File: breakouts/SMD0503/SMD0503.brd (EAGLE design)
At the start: 13.6 x 17.9 mm, 8 parts

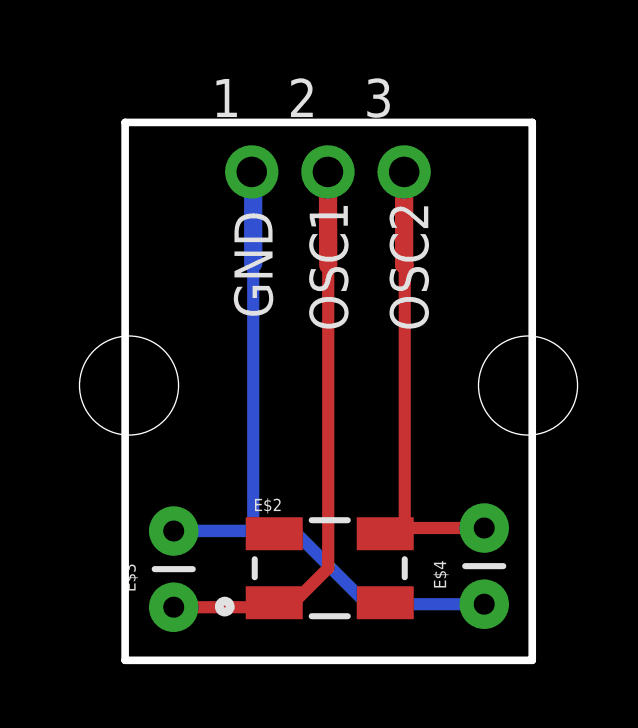
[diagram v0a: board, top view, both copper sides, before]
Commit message: SMD0503 - converted entirely to SMD components
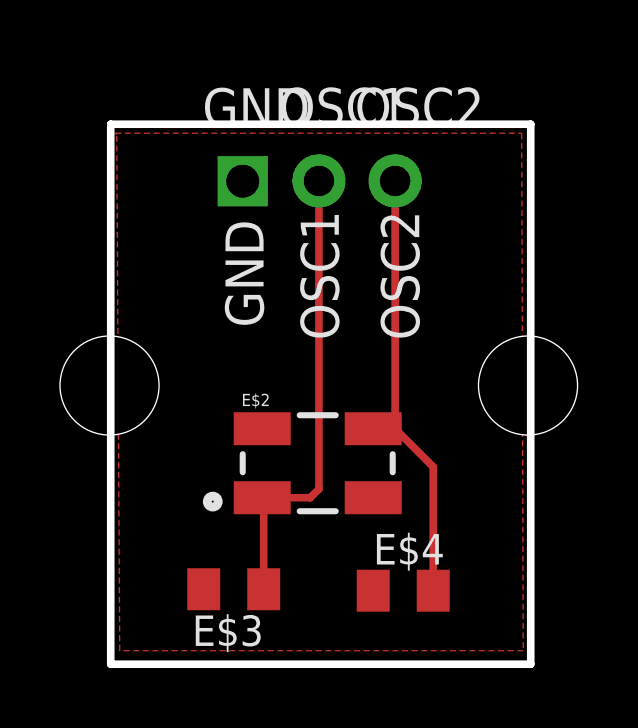
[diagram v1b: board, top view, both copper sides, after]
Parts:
- removed 1, 2, 3: (no value), adafruit:1X01-CLEANBIG
- added GND: (no value), adafruit_4u:1X01
- added OSC1, OSC2: (no value), adafruit:1X01-CLEANBIG
- E$3, E$4: device SparkFun:CAP-PTH-SMALL -> adafruit:C0805K
- moved E$2 3.52 mm to (14.9, 11.7)
- moved E$4 2.74 mm to (17.8, 7.45), turned to 0 degrees
- moved E$3 2.09 mm to (12.1, 7.50), turned to 180 degrees
- moved JP4 0.65 mm to (7.96, 14.3)
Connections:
- net GND: now also GND.1; no longer 1.1
- net OSC1: now also OSC1.1; no longer 2.1
- net OSC2: now also OSC2.1; no longer 3.1
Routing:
- net GND: track 26.0 -> 0.00 mm
- net OSC1: track 18.9 -> 15.4 mm
- added copper zone on layer 1, net GND
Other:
- board size 13.6 x 17.9 mm -> 14 x 18 mm
- board text added: "SMD0503"
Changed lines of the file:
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@@
 <layer number="45" name="Holes" color="7" fill="1" visible="no" active="yes"/>
 <layer number="46" name="Milling" color="3" fill="1" visible="no" active="yes"/>
-<layer number="47" name="Measures" color="7" fill="1" visible="no" active="yes"/>
+<layer number="47" name="Measures" color="7" fill="1" visible="yes" active="yes"/>
 <layer number="48" name="Document" color="7" fill="1" visible="yes" active="yes"/>
 <layer number="49" name="Reference" color="7" fill="1" visible="yes" active="yes"/>
@@
 <board>
 <plain>
-<wire x1="8.48" y1="5.13" x2="8.48" y2="23.06" width="0.254" layer="20"/>
-<wire x1="8.48" y1="23.06" x2="22.05" y2="23.06" width="0.254" layer="20"/>
-<wire x1="22.05" y1="23.06" x2="22.05" y2="5.13" width="0.254" layer="20"/>
-<wire x1="22.05" y1="5.13" x2="8.48" y2="5.13" width="0.254" layer="20"/>
-<text x="12.125" y="20.12" size="1.27" layer="121" font="vector" ratio="15" rot="R270">GND</text>
-<text x="14.635" y="20.42" size="1.27" layer="121" font="vector" ratio="15" rot="R270">OSC1</text>
-<text x="17.315" y="20.42" size="1.27" layer="121" font="vector" ratio="15" rot="R270">OSC2</text>
-<text x="19.93" y="18.03" size="1.27" layer="122" font="vector" rot="MR0">quilix.com</text>
+<wire x1="8" y1="5" x2="8" y2="23" width="0.254" layer="20"/>
+<wire x1="8" y1="23" x2="22" y2="23" width="0.254" layer="20"/>
+<wire x1="22" y1="23" x2="22" y2="5" width="0.254" layer="20"/>
+<wire x1="22" y1="5" x2="8" y2="5" width="0.254" layer="20"/>
+<text x="11.825" y="19.82" size="1.27" layer="121" font="vector" ratio="15" rot="R270">GND</text>
+<text x="14.335" y="20.12" size="1.27" layer="121" font="vector" ratio="15" rot="R270">OSC1</text>
+<text x="17.015" y="20.12" size="1.27" layer="121" font="vector" ratio="15" rot="R270">OSC2</text>
+<text x="19.63" y="17.93" size="1.27" layer="122" font="vector" ratio="10" rot="MR0">quilix.com</text>
+<text x="18.98" y="7.48" size="1.27" layer="122" font="vector" ratio="10" rot="MR0">SMD0503</text>
+<dimension x1="8" y1="23.06" x2="22" y2="23.06" x3="15" y3="28.3" layer="47"/>
+<dimension x1="8" y1="5.13" x2="15" y2="5.1" x3="11.47428125" y3="-0.885534375" layer="47"/>
+<dimension x1="8" y1="23" x2="8" y2="5" x3="0.05" y3="14" layer="47"/>
 </plain>
 <attributes>
@@
 <elements>
 <element name="JP3" library="SparkFun" package="STAND-OFF" value="STAND-OFF" x="21.91" y="14.29"/>
-<element name="JP4" library="SparkFun" package="STAND-OFF" value="STAND-OFF" x="8.61" y="14.29"/>
-<element name="1" library="adafruit" package="1X01-CLEANBIG" value="" x="12.7" y="21.41"/>
-<element name="2" library="adafruit" package="1X01-CLEANBIG" value="" x="15.24" y="21.41"/>
-<element name="3" library="adafruit" package="1X01-CLEANBIG" value="" x="17.78" y="21.41"/>
-<element name="E$2" library="SparkFun" package="CRYSTAL-OSC-SMD-5X3" value="" x="15.3" y="8.2"/>
-<element name="E$3" library="SparkFun" package="CAP-PTH-SMALL" value="" x="10.1" y="6.9" rot="R90"/>
-<element name="E$4" library="SparkFun" package="CAP-PTH-SMALL" value="" x="20.45" y="7" rot="R90"/>
+<element name="JP4" library="SparkFun" package="STAND-OFF" value="STAND-OFF" x="7.96" y="14.29"/>
+<element name="OSC1" library="adafruit" package="1X01-CLEANBIG" value="" x="14.94" y="21.11"/>
+<element name="OSC2" library="adafruit" package="1X01-CLEANBIG" value="" x="17.48" y="21.11"/>
+<element name="E$2" library="SparkFun" package="CRYSTAL-OSC-SMD-5X3" value="" x="14.9" y="11.7"/>
+<element name="E$3" library="adafruit" package="C0805K" value="" x="12.1" y="7.5" rot="R180"/>
+<element name="E$4" library="adafruit" package="C0805K" value="" x="17.75" y="7.45"/>
+<element name="GND" library="adafruit_4u" package="1X01" value="" x="12.4" y="21.1"/>
 </elements>
 <signals>
@@
 <contactref element="E$3" pad="1"/>
 <contactref element="E$2" pad="1"/>
-<contactref element="2" pad="1"/>
-<wire x1="10.1" y1="6.9" x2="13.3" y2="6.9" width="0.4064" layer="1"/>
-<wire x1="13.3" y1="6.9" x2="13.45" y2="7.05" width="0.4064" layer="1"/>
-<wire x1="15.24" y1="21.41" x2="15.25" y2="18.3" width="0.6096" layer="1"/>
-<wire x1="15.25" y1="18.3" x2="15.25" y2="8.2" width="0.4064" layer="1"/>
-<wire x1="15.25" y1="8.2" x2="14.1" y2="7.05" width="0.4064" layer="1"/>
-<wire x1="14.1" y1="7.05" x2="13.45" y2="7.05" width="0.4064" layer="1"/>
+<contactref element="OSC1" pad="1"/>
+<wire x1="13.05" y1="10.55" x2="13.1" y2="10.5" width="0.254" layer="1"/>
+<wire x1="13.1" y1="10.5" x2="13.1" y2="7.5" width="0.254" layer="1"/>
+<wire x1="14.94" y1="21.11" x2="14.94" y2="10.84" width="0.254" layer="1"/>
+<wire x1="14.94" y1="10.84" x2="14.65" y2="10.55" width="0.254" layer="1"/>
+<wire x1="14.65" y1="10.55" x2="13.05" y2="10.55" width="0.254" layer="1"/>
 </signal>
 <signal name="OSC2">
 <contactref element="E$4" pad="2"/>
 <contactref element="E$2" pad="3"/>
-<contactref element="3" pad="1"/>
-<wire x1="20.45" y1="9.54" x2="17.7" y2="9.54" width="0.4064" layer="1"/>
-<wire x1="17.7" y1="9.54" x2="17.34" y2="9.54" width="0.4064" layer="1"/>
-<wire x1="17.34" y1="9.54" x2="17.15" y2="9.35" width="0.4064" layer="1"/>
-<wire x1="17.78" y1="21.41" x2="17.78" y2="18.32" width="0.6096" layer="1"/>
-<wire x1="17.78" y1="18.32" x2="17.8" y2="18.3" width="0.6096" layer="1"/>
-<wire x1="17.8" y1="18.3" x2="17.8" y2="9.64" width="0.4064" layer="1"/>
-<wire x1="17.8" y1="9.64" x2="17.7" y2="9.54" width="0.4064" layer="1"/>
+<contactref element="OSC2" pad="1"/>
+<wire x1="17.48" y1="21.11" x2="17.48" y2="12.85" width="0.254" layer="1"/>
+<wire x1="17.48" y1="12.85" x2="16.75" y2="12.85" width="0.254" layer="1"/>
+<wire x1="17.48" y1="12.85" x2="18.75" y2="11.58" width="0.254" layer="1"/>
+<wire x1="18.75" y1="11.58" x2="18.75" y2="7.45" width="0.254" layer="1"/>
 </signal>
 <signal name="GND">
 <contactref element="E$4" pad="1"/>
 <contactref element="E$3" pad="2"/>
-<contactref element="1" pad="1"/>
-<wire x1="12.7" y1="21.41" x2="12.75" y2="21.41" width="0.6096" layer="16"/>
-<wire x1="12.75" y1="21.41" x2="12.75" y2="18.35" width="0.6096" layer="16"/>
-<wire x1="12.75" y1="18.35" x2="12.75" y2="9.44" width="0.4064" layer="16"/>
-<wire x1="12.75" y1="9.44" x2="10.1" y2="9.44" width="0.4064" layer="16"/>
-<wire x1="10.1" y1="9.44" x2="10.1" y2="9.45" width="0.4064" layer="16"/>
-<wire x1="10.1" y1="9.45" x2="14.1" y2="9.45" width="0.4064" layer="16"/>
-<wire x1="14.1" y1="9.45" x2="16.55" y2="7" width="0.4064" layer="16"/>
-<wire x1="16.55" y1="7" x2="20.45" y2="7" width="0.4064" layer="16"/>
+<polygon width="0.254" layer="1">
+<vertex x="8.15" y="22.7"/>
+<vertex x="21.7" y="22.7"/>
+<vertex x="21.75" y="5.45"/>
+<vertex x="8.3" y="5.45"/>
+<vertex x="8.2" y="22.65"/>
+</polygon>
+<contactref element="GND" pad="1"/>
 </signal>
 </signals>
